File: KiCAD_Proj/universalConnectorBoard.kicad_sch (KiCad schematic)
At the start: 40 parts, among them IC1 RPI_Pico_EvaluationBoard, IC2 SN74LV4052ADR, IC4 TCA9534DWR, J1 691401700003B, J10 Cheeks, J11 MD_SW1, J12 MD_SW2, J13 Motor1, J14 Motor2, J15 Conn_01x02_Pin, J2 Display1, J3 Display2, J4 RPI4, J5 Ledstrip2, J6 MUX3_UART, J7 MUX4_UART, J8 Ledstrip1, J9 Mouth

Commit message: Finished schematic, in review
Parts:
- removed J13: Motor1, Connector_JST:JST_XH_S6B-XH-A_1x06_P2.50mm_Horizontal, symbol Connector:Conn_01x06_Pin
- removed J14: Motor2, Connector_JST:JST_XH_S6B-XH-A_1x06_P2.50mm_Horizontal, symbol Connector:Conn_01x06_Pin
- removed J6: MUX3_UART, Connector_PinSocket_2.54mm:PinSocket_1x04_P2.54mm_Vertical, symbol Connector:Conn_01x04_Pin
- removed J7: MUX4_UART, Connector_PinSocket_2.54mm:PinSocket_1x04_P2.54mm_Vertical, symbol Connector:Conn_01x04_Pin
- added C19, C20, C21: 0.10μF, Capacitor_SMD:C_0603_1608Metric_Pad1.08x0.95mm_HandSolder, symbol Device:C
- added D1: LED, LED_SMD:LED_0603_1608Metric_Pad1.05x0.95mm_HandSolder, symbol Device:LED
- added J13: Motor1, Connector_JST:JST_XH_S4B-XH-A_1x04_P2.50mm_Horizontal, symbol Connector:Conn_01x04_Pin
- added J14: Motor2, Connector_JST:JST_XH_S4B-XH-A_1x04_P2.50mm_Horizontal, symbol Connector:Conn_01x04_Pin
- added J15: Extra VCC/GND, Connector_PinHeader_2.54mm:PinHeader_2x03_P2.54mm_Vertical, symbol Connector_Generic:Conn_02x03_Top_Bottom
- added J6: Extra MUX_UART, Connector_PinHeader_2.54mm:PinHeader_2x04_P2.54mm_Vertical, symbol Connector_Generic:Conn_02x04_Top_Bottom
- added JP6, JP7: Ledstrip_VCC, Connector_PinHeader_2.54mm:PinHeader_1x03_P2.54mm_Vertical, symbol Jumper:Jumper_3_Bridged12
- added Q1, Q2: 2N7002, Package_TO_SOT_SMD:SOT-23, symbol Transistor_FET:2N7002
- added Q3: BSS84, Package_TO_SOT_SMD:SOT-23, symbol Transistor_FET:BSS84
- added R26: 47, Resistor_SMD:R_0603_1608Metric_Pad0.98x0.95mm_HandSolder, symbol Device:R
- added R27, R30: 100, Resistor_SMD:R_0603_1608Metric_Pad0.98x0.95mm_HandSolder, symbol Device:R
- added R28: 50k, Resistor_SMD:R_0603_1608Metric_Pad0.98x0.95mm_HandSolder, symbol Device:R
- added R29: 75, Resistor_SMD:R_0603_1608Metric_Pad0.98x0.95mm_HandSolder, symbol Device:R
- added SW1: SW_Push, Connector_PinHeader_2.54mm:PinHeader_1x02_P2.54mm_Vertical, symbol Switch:SW_Push
- J4: footprint Connector_PinHeader_2.54mm:PinHeader_2x20_P2.54mm_Vertical_SMD -> Connector_PinHeader_2.54mm:PinHeader_2x20_P2.54mm_Vertical
- J7: renamed from J15; value Conn_01x02_Pin -> Extra GPIO output; footprint (none) -> Connector_PinHeader_2.54mm:PinHeader_1x02_P2.54mm_Vertical
- JP1: renamed from JP2; value Jumper_3_Bridged12 -> Mux_Vcc
- R22: value R -> 47
- R23: value R -> 50k
- R24, R25: value 10k -> 50k
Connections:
- net MUX_TX4 is gone; now on net MUX_RX4: IC2.11 (1Y3), R4.2
- net +12V: now also J15.3 (Pin_3), JP6.1 (A), JP7.1 (A); no longer C2.2, J8.4 (Pin_4)
- net +3.3V: now also C21.2, J15.1 (Pin_1), Q3.3 (D)
- net +5V: now also D1.2 (A), J15.2 (Pin_2), JP6.3 (B), JP7.3 (B), Q1.3 (D), Q2.3 (D); no longer C3.2, J5.3 (Pin_3)
- net GND: now also R23.2, C19.2, C20.2, J15.4 (Pin_4), J15.5 (Pin_5), J15.6 (Pin_6), J6.4 (Pin_4), J6.8 (Pin_8), R27.2, R28.2, R29.2, R30.1, SW1.1; no longer R22.1, R23.1
- net LED_Cheeks: now also R22.1; no longer J9.1 (Pin_1)
- net LED_Mouth: now also R26.1; no longer J10.1 (Pin_1)
- net MUX_RX3: now also J6.7 (Pin_7)
- net MUX_RX4: now also J6.2 (Pin_2), J6.3 (Pin_3)
- net MUX_TX3: now also J6.6 (Pin_6)
- net Regulator5V/GND: now also C21.1
- net StepperMotors/MD1_A1: now also J13.4 (Pin_4)
- net StepperMotors/MD1_A2: now also J13.3 (Pin_3)
- net StepperMotors/MD1_B1: now also J13.2 (Pin_2)
- net StepperMotors/MD1_B2: now also J13.1 (Pin_1)
- net StepperMotors/MD2_A1: now also J14.4 (Pin_4)
- net StepperMotors/MD2_A2: now also J14.3 (Pin_3)
- net StepperMotors/MD2_B1: now also J14.2 (Pin_2)
- net StepperMotors/MD2_B2: now also J14.1 (Pin_1)
- net VCC_MUX: now also J6.1 (Pin_1), J6.5 (Pin_5)
- net at J9.2 (Pin_2): now also R27.1; no longer R23.2
- net SWCLK: now reaches J4.18 (Pin_18)
- net SWCLK: now also IC1.41 (SWCLK)
- net SWDIO: now reaches J4.22 (Pin_22)
- net SWDIO: now also IC1.43 (SWDIO)
- net at J4.36 (Pin_36): now also SW1.2
- net at IC1.39 (VSYS): now also Q3.2 (S)
- net at IC1.40 (VBUS): now also Q3.1 (G)
- net MUX_GPIO6: now reaches IC4.11 (P6)
- net MUX_GPIO6: now also J7.1 (Pin_1)
- net MUX_GPIO7: now reaches IC4.12 (P7)
- net MUX_GPIO7: now also J7.2 (Pin_2)
- net at J10.2 (Pin_2): now also R29.1; no longer R22.2
- new net: Q2.1 (G), R22.2, R23.1
- new net: J10.1 (Pin_1), Q2.2 (S)
- new net: Q1.1 (G), R26.2, R28.1
- new net: J9.1 (Pin_1), Q1.2 (S)
- new net: D1.1 (K), R30.2
- new net VCC_STRIP: C2.2, J8.4 (Pin_4)
- new net VCC_STRIP1: C19.1, JP6.2 (C)
- new net VCC_STRIP2: C20.1, C3.2, J5.3 (Pin_3), JP7.2 (C)
- no-connect marks 0 -> 29
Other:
- sheet StepperMotors ports: added 12V+, 3.3V+; removed none
- note added: "1) Most connectors are JST, please check if this is doable for all components (ledstrips have black connectors already, maybe a connector that fits those?)"
- note added: "2) Before making all the traces, where should every component be? I placed all components (except for small ones) roughly on the PCB editor. Where do we want which connector (e.g.)?"
- note added: "Extra"
- note added: "GPIO16"
- note added: "Notes"
- note added: "SN1: If you are sure about an error, don't hesitate to change it! If not sure, list is as an potential error in your feedback."
- note added: "SN2: Every type of feedback is appreciated, but keep in mind, that this is my very first PCB design, so be kind :)"
- note removed: "2) Connectoren: leds, ledstrips, motoren 3) Shutdown button PI4? 4) 4,7 of 100k voor mux uart 5) Weerstandwaarde R22/R33 (kleur led?? 100/150) 6) Connector motoren? 4 of 6 pins"
- note removed: "3.3V ?? 12V ??"
- note removed: "4,7 of 100k?"
- note removed: "Extra uart"
- note removed: "Shutdown button??"
- note removed: "Vsys?"
- moved on the sheet: C2, C3, IC1, J2, J3, J4, J5, J7, J8, J9, R10, R9

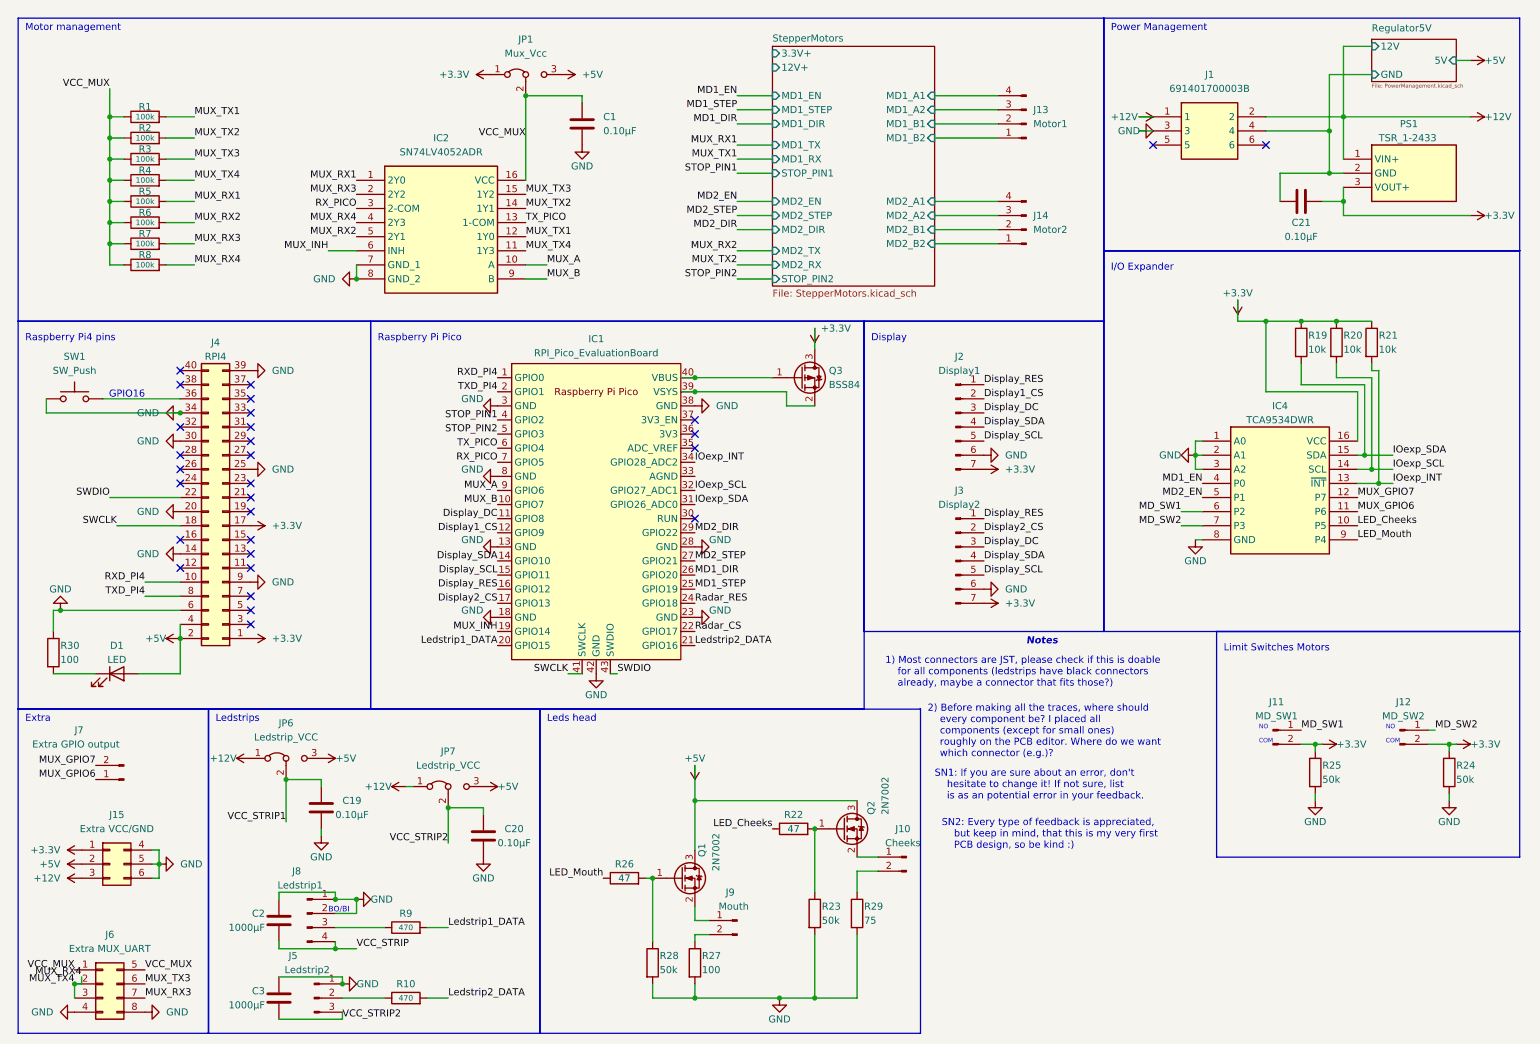
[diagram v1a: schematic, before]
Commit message: -add missing connections in schematic, and some other small changes
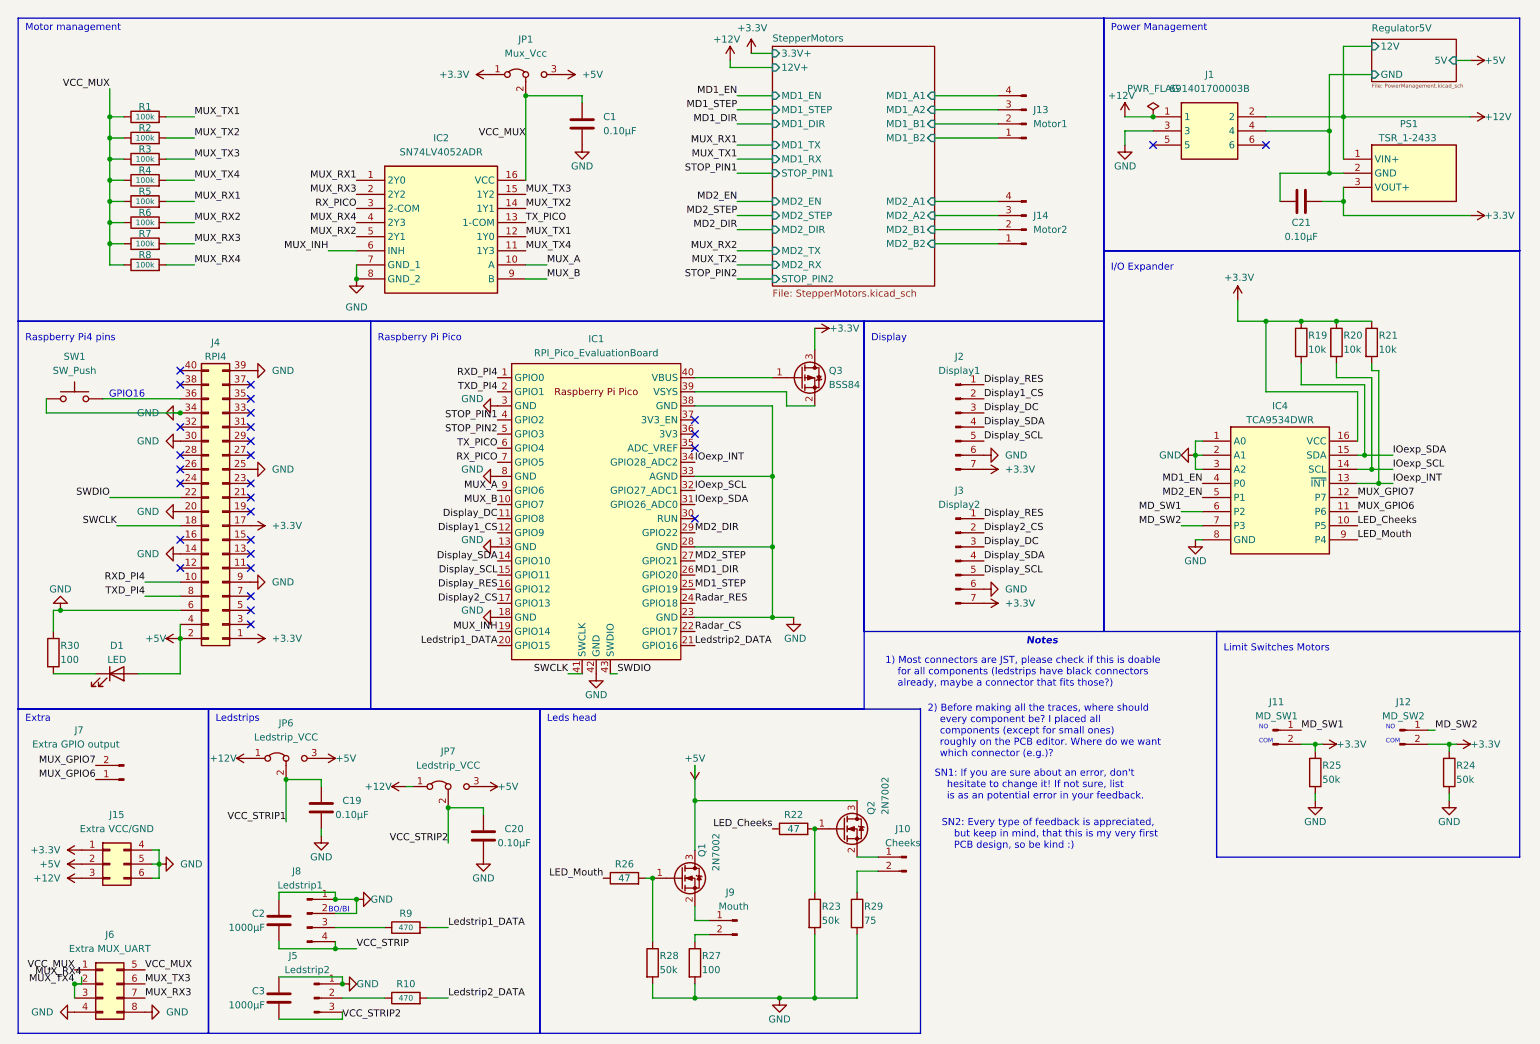
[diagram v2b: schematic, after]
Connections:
- net GND: now also IC1.33 (AGND)

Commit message: Schematic finished
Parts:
- removed J7: Extra GPIO output, Connector_PinHeader_2.54mm:PinHeader_1x02_P2.54mm_Vertical, symbol Connector:Conn_01x02_Pin
- added C22: 100nF, Capacitor_SMD:C_0603_1608Metric_Pad1.08x0.95mm_HandSolder, symbol Device:C
- added J7: Radar, symbol Connector:Conn_01x08_Pin
- added R31: 4.7k, Resistor_SMD:R_0603_1608Metric_Pad0.98x0.95mm_HandSolder, symbol Device:R
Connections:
- net MUX_GPIO6 is gone; now on net MUX_B: IC4.11 (P6)
- net MUX_GPIO7 is gone; now on net MUX_A: IC4.12 (P7)
- net +3.3V: now also J7.7 (Pin_7)
- net Display_RES: now also IC1.10 (GPIO7); no longer IC1.16 (GPIO12)
- net Display_SCL: no longer IC1.15 (GPIO11)
- net Display_SDA: no longer IC1.14 (GPIO10)
- net GND: now also C22.2, J7.6 (Pin_6); no longer SW1.1
- net LED_Cheeks: now also R22.2; no longer R22.1
- net LED_Mouth: now also R26.2; no longer R26.1
- net MUX_A: no longer IC1.9 (GPIO6)
- net MUX_B: no longer IC1.10 (GPIO7)
- net MUX_RX4: no longer IC2.11 (1Y3), J6.3 (Pin_3), R4.2
- net Radar_CS: now also J7.2 (Pin_2)
- net Radar_RES: now also J7.1 (Pin_1)
- net at Q2.1 (G), R23.1: now also R22.1; no longer R22.2
- net at Q1.1 (G), R28.1: now also R26.1; no longer R26.2
- new net: C22.1, R31.1
- new net: R31.2, SW1.1
- new net Display_CLK: IC1.14 (GPIO10), J7.3 (Pin_3)
- new net Display_MOSI: IC1.15 (GPIO11), J7.4 (Pin_4)
- new net MUX_TX4: IC2.11 (1Y3), J6.3 (Pin_3), R4.2
- new net Radar_INT: IC1.9 (GPIO6), J7.8 (Pin_8)
- new net Radar_MISO: IC1.16 (GPIO12), J7.5 (Pin_5)
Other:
- sheet StepperMotors ports: added none; removed 12V+, 3.3V+
- note added: "Radar"
- moved on the sheet: C19, C2, C20, C21, C3, D1, IC1, IC4, J1, J10, J11, J12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

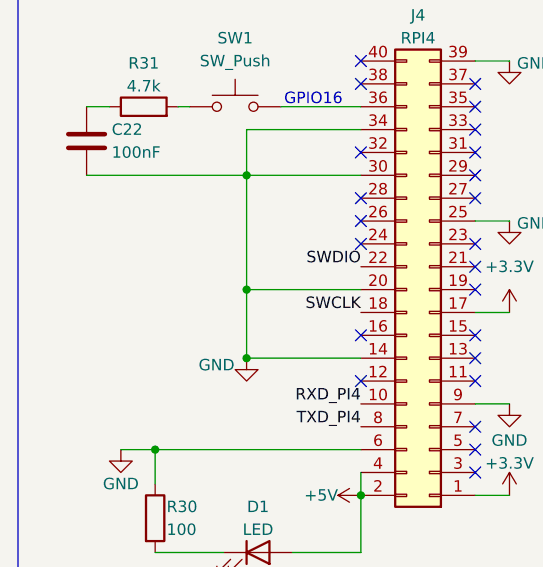
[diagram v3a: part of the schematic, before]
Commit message: Added Pi HAT reference footprint
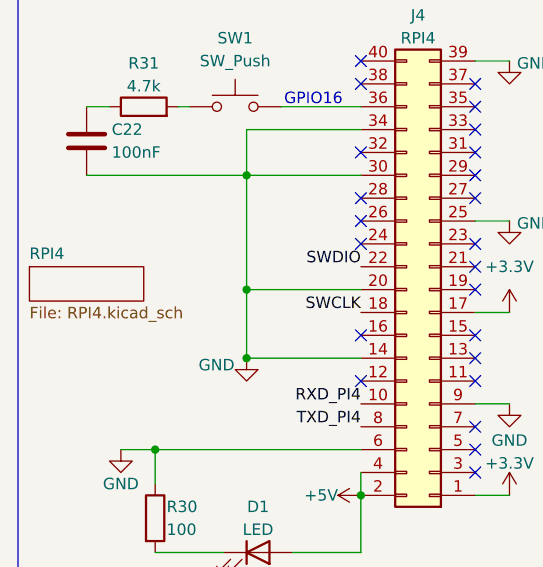
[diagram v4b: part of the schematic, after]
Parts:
- J7: footprint (none) -> Connector_JST:JST_XH_S8B-XH-A_1x08_P2.50mm_Horizontal
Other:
- added sheet RPI4 (RPI4.kicad_sch)
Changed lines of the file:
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@@
 			)
 		)
-		(property "Footprint" ""
+		(property "Footprint" "Connector_JST:JST_XH_S8B-XH-A_1x08_P2.50mm_Horizontal"
 			(at 189.23 152.4 0)
 			(effects
@@
 				)
 			)
+		)
+	)
+	(sheet
+		(at 15.24 106.68)
+		(size 12.7 3.81)
+		(fields_autoplaced yes)
+		(stroke
+			(width 0.1524)
+			(type solid)
+		)
+		(fill
+			(color 0 0 0 0.0000)
+		)
+		(property "Sheetname" "RPI4"
+			(at 15.24 105.9684 0)
+			(effects
+				(font
+					(size 1.27 1.27)
+				)
+				(justify left bottom)
+			)
+		)
+		(property "Sheetfile" "RPI4.kicad_sch"
+			(at 15.24 111.0746 0)
+			(effects
+				(font
+					(size 1.27 1.27)
+				)
+				(justify left top)
+			)
+		)
+		(instances
+			(project "universalConnectorBoard"
+				(path "/4d36baa7-ef48-416a-b1c8-6a662c0af28f"
+					(page "4")
+				)
+			)
